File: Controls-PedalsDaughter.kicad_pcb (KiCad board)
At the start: 2 copper layers, 40 x 50 mm, 37 parts, among them J2 Accel Pos. Sensor, J3 PeripheralCANConnector, J4 Conn_01x02, J5 PeripheralCANConnector, U1 RI3-1205S, U2 PeripheralSOM, U3 TLV9301xDCK, U4 AMC1300BDWV, U5 TLV70130DBVR

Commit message: again
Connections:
- D1 pad 1: +3.3V -> +3V3
- D3 pad 1: +3.3V -> +3V3
- U2 pad 2: +3.3V -> +3V3
- U2 pad 9: +3.3V -> +3V3
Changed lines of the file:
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@@
 	(net 7 "+3V3PWR")
 	(net 8 "+3V3")
-	(net 9 "+3.3V")
-	(net 10 "Net-(D6-A)")
-	(net 11 "unconnected-(J2-Pin_2-Pad2)")
-	(net 12 "Net-(J2-Pin_5)")
-	(net 13 "/CAN_L")
-	(net 14 "/CAN_H")
-	(net 15 "/INP")
-	(net 16 "Net-(U3-+)")
-	(net 17 "unconnected-(U2-SPI1_NSS-Pad19)")
-	(net 18 "unconnected-(U2-I2C2_SCL-Pad8)")
-	(net 19 "unconnected-(U2-SPI1_MISO-Pad15)")
-	(net 20 "unconnected-(U2-VDDA(3.3V)-Pad10)")
-	(net 21 "unconnected-(U2-SPI2_NSS-Pad7)")
-	(net 22 "unconnected-(U2-GNDA-Pad12)")
-	(net 23 "unconnected-(U2-SPI1_SCK-Pad13)")
-	(net 24 "unconnected-(U2-SPI2_MOSI-Pad1)")
-	(net 25 "unconnected-(U2-SPI2_MISO-Pad3)")
-	(net 26 "unconnected-(U2-I2C1_SDA-Pad16)")
-	(net 27 "unconnected-(U2-I2C2_SDA-Pad6)")
-	(net 28 "unconnected-(U2-SPI2_SCK-Pad5)")
-	(net 29 "unconnected-(U2-SPI1_MOSI-Pad17)")
-	(net 30 "unconnected-(U2-I2C1_SCL-Pad14)")
-	(net 31 "unconnected-(U5-NC-Pad3)")
-	(net 32 "unconnected-(U5-NC-Pad2)")
+	(net 9 "Net-(D6-A)")
+	(net 10 "unconnected-(J2-Pin_2-Pad2)")
+	(net 11 "Net-(J2-Pin_5)")
+	(net 12 "/CAN_L")
+	(net 13 "/CAN_H")
+	(net 14 "/INP")
+	(net 15 "Net-(U3-+)")
+	(net 16 "unconnected-(U2-SPI1_NSS-Pad19)")
+	(net 17 "unconnected-(U2-I2C2_SCL-Pad8)")
+	(net 18 "unconnected-(U2-SPI1_MISO-Pad15)")
+	(net 19 "unconnected-(U2-VDDA(3.3V)-Pad10)")
+	(net 20 "unconnected-(U2-SPI2_NSS-Pad7)")
+	(net 21 "unconnected-(U2-GNDA-Pad12)")
+	(net 22 "unconnected-(U2-SPI1_SCK-Pad13)")
+	(net 23 "unconnected-(U2-SPI2_MOSI-Pad1)")
+	(net 24 "unconnected-(U2-SPI2_MISO-Pad3)")
+	(net 25 "unconnected-(U2-I2C1_SDA-Pad16)")
+	(net 26 "unconnected-(U2-I2C2_SDA-Pad6)")
+	(net 27 "unconnected-(U2-SPI2_SCK-Pad5)")
+	(net 28 "unconnected-(U2-SPI1_MOSI-Pad17)")
+	(net 29 "unconnected-(U2-I2C1_SCL-Pad14)")
+	(net 30 "unconnected-(U5-NC-Pad3)")
+	(net 31 "unconnected-(U5-NC-Pad2)")
 	(footprint "TestPoint:TestPoint_Pad_1.5x1.5mm"
 		(layer "F.Cu")
@@
 			(layers "*.Cu" "*.Mask")
 			(remove_unused_layers no)
-			(net 14 "/CAN_H")
+			(net 13 "/CAN_H")
 			(pinfunction "CAN_H")
 			(pintype "bidirectional")
@@
 			(layers "*.Cu" "*.Mask")
 			(remove_unused_layers no)
-			(net 13 "/CAN_L")
+			(net 12 "/CAN_L")
 			(pinfunction "CAN_L")
 			(pintype "bidirectional")
@@
 			(layers "F.Cu" "F.Paste" "F.Mask")
 			(roundrect_rratio 0.25)
-			(net 16 "Net-(U3-+)")
+			(net 15 "Net-(U3-+)")
 			(pinfunction "+")
 			(pintype "input")
@@
 			(layers "F.Cu" "F.Paste" "F.Mask")
 			(roundrect_rratio 0.25)
-			(net 32 "unconnected-(U5-NC-Pad2)")
+			(net 31 "unconnected-(U5-NC-Pad2)")
 			(pinfunction "NC")
 			(pintype "unspecified+no_connect")
@@
 			(layers "F.Cu" "F.Paste" "F.Mask")
 			(roundrect_rratio 0.25)
-			(net 31 "unconnected-(U5-NC-Pad3)")
+			(net 30 "unconnected-(U5-NC-Pad3)")
 			(pinfunction "NC")
 			(pintype "unspecified+no_connect")
@@
 			(layers "*.Cu" "*.Mask")
 			(remove_unused_layers no)
-			(net 11 "unconnected-(J2-Pin_2-Pad2)")
+			(net 10 "unconnected-(J2-Pin_2-Pad2)")
 			(pinfunction "Pin_2")
 			(pintype "passive+no_connect")
@@
 			(layers "*.Cu" "*.Mask")
 			(remove_unused_layers no)
-			(net 12 "Net-(J2-Pin_5)")
+			(net 11 "Net-(J2-Pin_5)")
 			(pinfunction "Pin_5")
 			(pintype "passive")
@@
 			(layers "*.Cu" "*.Mask")
 			(remove_unused_layers no)
-			(net 14 "/CAN_H")
+			(net 13 "/CAN_H")
 			(pinfunction "CAN_H")
 			(pintype "bidirectional")
@@
 			(layers "*.Cu" "*.Mask")
 			(remove_unused_layers no)
-			(net 13 "/CAN_L")
+			(net 12 "/CAN_L")
 			(pinfunction "CAN_L")
 			(pintype "bidirectional")
@@
 			(layers "F.Cu" "F.Paste" "F.Mask")
 			(roundrect_rratio 0.25)
-			(net 15 "/INP")
+			(net 14 "/INP")
 			(pinfunction "+")
 			(pintype "input")
@@
 			(layers "F.Cu" "F.Paste" "F.Mask")
 			(roundrect_rratio 0.25)
-			(net 10 "Net-(D6-A)")
+			(net 9 "Net-(D6-A)")
 			(pinfunction "A")
 			(pintype "passive")
@@
 			(layers "*.Cu" "*.Mask")
 			(remove_unused_layers no)
-			(net 15 "/INP")
+			(net 14 "/INP")
 			(pinfunction "Pin_2")
 			(pintype "passive")
@@
 			(layers "B.Cu" "B.Paste" "B.Mask")
 			(roundrect_rratio 0.25)
-			(net 9 "+3.3V")
+			(net 8 "+3V3")
 			(pinfunction "K")
 			(pintype "passive")
@@
 			(layers "B.Cu" "B.Paste" "B.Mask")
 			(roundrect_rratio 0.243902)
-			(net 16 "Net-(U3-+)")
+			(net 15 "Net-(U3-+)")
 			(pintype "passive")
 		)
@@
 			(layers "B.Cu" "B.Paste" "B.Mask")
 			(roundrect_rratio 0.243902)
-			(net 12 "Net-(J2-Pin_5)")
+			(net 11 "Net-(J2-Pin_5)")
 			(pintype "passive")
 		)
@@
 			(layers "B.Cu" "B.Paste" "B.Mask")
 			(roundrect_rratio 0.243902)
-			(net 16 "Net-(U3-+)")
+			(net 15 "Net-(U3-+)")
 			(pintype "passive")
 		)
@@
 			(layers "B.Cu" "B.Paste" "B.Mask")
 			(roundrect_rratio 0.243902)
-			(net 10 "Net-(D6-A)")
+			(net 9 "Net-(D6-A)")
 			(pintype "passive")
 		)
@@
 			(layers "B.Cu" "B.Paste" "B.Mask")
 			(roundrect_rratio 0.243902)
-			(net 15 "/INP")
+			(net 14 "/INP")
 			(pintype "passive")
 		)
@@
 		(fp_arc
 			(start 21.237742 18.612258)
-			(mid 20.300482 20.874999)
+			(mid 20.300481 20.874995)
 			(end 18.037742 21.812258)
 			(stroke
@@
 			(size 0.55 1.8)
 			(layers "B.Cu" "B.Paste" "B.Mask")
-			(net 24 "unconnected-(U2-SPI2_MOSI-Pad1)")
+			(net 23 "unconnected-(U2-SPI2_MOSI-Pad1)")
 			(pinfunction "SPI2_MOSI")
 			(pintype "passive+no_connect")
 		)
 		(pad "2" smd rect
-			(at 20.475 1.175 90)
+			(at 20.475 1.175 270)
 			(size 0.55 1.8)
 			(layers "B.Cu" "B.Paste" "B.Mask")
-			(net 9 "+3.3V")
+			(net 8 "+3V3")
 			(pinfunction "+3.3V")
 			(pintype "passive")
@@
 			(size 0.55 1.8)
 			(layers "B.Cu" "B.Paste" "B.Mask")
-			(net 25 "unconnected-(U2-SPI2_MISO-Pad3)")
+			(net 24 "unconnected-(U2-SPI2_MISO-Pad3)")
 			(pinfunction "SPI2_MISO")
 			(pintype "passive+no_connect")
@@
 			(size 0.55 1.8)
 			(layers "B.Cu" "B.Paste" "B.Mask")
-			(net 28 "unconnected-(U2-SPI2_SCK-Pad5)")
+			(net 27 "unconnected-(U2-SPI2_SCK-Pad5)")
 			(pinfunction "SPI2_SCK")
 			(pintype "passive+no_connect")
@@
 			(size 0.55 1.8)
 			(layers "B.Cu" "B.Paste" "B.Mask")
-			(net 27 "unconnected-(U2-I2C2_SDA-Pad6)")
+			(net 26 "unconnected-(U2-I2C2_SDA-Pad6)")
 			(pinfunction "I2C2_SDA")
 			(pintype "passive+no_connect")
@@
 			(size 0.55 1.8)
 			(layers "B.Cu" "B.Paste" "B.Mask")
-			(net 21 "unconnected-(U2-SPI2_NSS-Pad7)")
+			(net 20 "unconnected-(U2-SPI2_NSS-Pad7)")
 			(pinfunction "SPI2_NSS")
 			(pintype "passive+no_connect")
@@
 			(size 0.55 1.8)
 			(layers "B.Cu" "B.Paste" "B.Mask")
-			(net 18 "unconnected-(U2-I2C2_SCL-Pad8)")
+			(net 17 "unconnected-(U2-I2C2_SCL-Pad8)")
 			(pinfunction "I2C2_SCL")
 			(pintype "passive+no_connect")
 		)
 		(pad "9" smd rect
-			(at 16.175 -2.025 90)
+			(at 16.175 -2.025 270)
 			(size 0.55 1.8)
 			(layers "B.Cu" "B.Paste" "B.Mask")
-			(net 9 "+3.3V")
+			(net 8 "+3V3")
 			(pinfunction "+3.3V")
 			(pintype "output")
@@
 			(size 0.55 1.8)
 			(layers "B.Cu" "B.Paste" "B.Mask")
-			(net 20 "unconnected-(U2-VDDA(3.3V)-Pad10)")
+			(net 19 "unconnected-(U2-VDDA(3.3V)-Pad10)")
 			(pinfunction "VDDA(3.3V)")
 			(pintype "passive+no_connect")
@@
 			(size 0.55 1.8)
 			(layers "B.Cu" "B.Paste" "B.Mask")
-			(net 22 "unconnected-(U2-GNDA-Pad12)")
+			(net 21 "unconnected-(U2-GNDA-Pad12)")
 			(pinfunction "GNDA")
 			(pintype "output+no_connect")
@@
 			(size 0.55 1.8)
 			(layers "B.Cu" "B.Paste" "B.Mask")
-			(net 23 "unconnected-(U2-SPI1_SCK-Pad13)")
+			(net 22 "unconnected-(U2-SPI1_SCK-Pad13)")
 			(pinfunction "SPI1_SCK")
 			(pintype "passive+no_connect")
@@
 			(size 0.55 1.8)
 			(layers "B.Cu" "B.Paste" "B.Mask")
-			(net 30 "unconnected-(U2-I2C1_SCL-Pad14)")
+			(net 29 "unconnected-(U2-I2C1_SCL-Pad14)")
 			(pinfunction "I2C1_SCL")
 			(pintype "passive+no_connect")
@@
 			(size 0.55 1.8)
 			(layers "B.Cu" "B.Paste" "B.Mask")
-			(net 19 "unconnected-(U2-SPI1_MISO-Pad15)")
+			(net 18 "unconnected-(U2-SPI1_MISO-Pad15)")
 			(pinfunction "SPI1_MISO")
 			(pintype "passive+no_connect")
@@
 			(size 0.55 1.8)
 			(layers "B.Cu" "B.Paste" "B.Mask")
-			(net 26 "unconnected-(U2-I2C1_SDA-Pad16)")
+			(net 25 "unconnected-(U2-I2C1_SDA-Pad16)")
 			(pinfunction "I2C1_SDA")
 			(pintype "passive+no_connect")
@@
 			(size 0.55 1.8)
 			(layers "B.Cu" "B.Paste" "B.Mask")
-			(net 29 "unconnected-(U2-SPI1_MOSI-Pad17)")
+			(net 28 "unconnected-(U2-SPI1_MOSI-Pad17)")
 			(pinfunction "SPI1_MOSI")
 			(pintype "passive+no_connect")
@@
 			(size 0.55 1.8)
 			(layers "B.Cu" "B.Paste" "B.Mask")
-			(net 17 "unconnected-(U2-SPI1_NSS-Pad19)")
+			(net 16 "unconnected-(U2-SPI1_NSS-Pad19)")
 			(pinfunction "SPI1_NSS")
 			(pintype "passive+no_connect")
@@
 			(size 0.55 1.8)
 			(layers "B.Cu" "B.Paste" "B.Mask")
-			(net 13 "/CAN_L")
+			(net 12 "/CAN_L")
 			(pinfunction "CAN_L")
 			(pintype "passive")
@@
 			(size 0.55 1.8)
 			(layers "B.Cu" "B.Paste" "B.Mask")
-			(net 14 "/CAN_H")
+			(net 13 "/CAN_H")
 			(pinfunction "CAN_H")
 			(pintype "passive")
@@
 			(layers "B.Cu" "B.Paste" "B.Mask")
 			(roundrect_rratio 0.25)
-			(net 9 "+3.3V")
+			(net 8 "+3V3")
 			(pinfunction "K")
 			(pintype "passive")

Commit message: Yuh
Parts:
- added Accel_Raw1: Accel_Raw_TP, TestPoint:TestPoint_THTPad_1.5x1.5mm_Drill0.7mm, F.Cu at (101.8, 76.5)
- added Accel_TP1: Accel, TestPoint:TestPoint_THTPad_1.5x1.5mm_Drill0.7mm, F.Cu at (106.6, 67.5)
- added Brake_Fl_Sn1: Brake_Fl_Sn_TP, TestPoint:TestPoint_THTPad_1.5x1.5mm_Drill0.7mm, F.Cu at (123.0, 66.8)
- added Brake_Fl_Sn_Raw1: Brake_Fl_Sn_Raw_TP, TestPoint:TestPoint_THTPad_1.5x1.5mm_Drill0.7mm, F.Cu at (124.2, 47.0)
- added Brake_Raw1: Brake_Raw_TP, TestPoint:TestPoint_THTPad_1.5x1.5mm_Drill0.7mm, F.Cu at (101.8, 50.2)
- added Brake_TP1: Brake, TestPoint:TestPoint_THTPad_1.5x1.5mm_Drill0.7mm, F.Cu at (106.5, 59.0)
- added C13: 0.1uf, Capacitor_SMD:C_0805_2012Metric, F.Cu at (109.1, 53.7)
- added C14: 1nf, Capacitor_SMD:C_0805_2012Metric, F.Cu at (104.1, 53.7)
- added D5: MBR, Diode_SMD:D_0805_2012Metric, F.Cu at (104.8, 56.5)
- added D8: MBR, Diode_SMD:D_0805_2012Metric, F.Cu at (108.4, 56.5)
- added J1: Brake Pos. Sensor, Connector_Molex:Molex_Micro-Fit_3.0_43045-0612_2x03_P3.00mm_Vertical, F.Cu at (104.6, 41.5)
- added R5: 8.2k, Resistor_SMD:R_0805_2012Metric, F.Cu at (107.5, 50.2)
- added R6: 22k, Resistor_SMD:R_0805_2012Metric, F.Cu at (105.5, 50.2)
- added U6: TLV9301xDCK, Package_TO_SOT_SMD:SOT-353_SC-70-5, F.Cu at (106.6, 53.7)
- C1: value 1nF -> 100nF; moved to F.Cu
- C10: value 1nF -> 1uF; moved to F.Cu
- C11: value 100nF -> 100uF; moved to F.Cu
- C12: value 0.1uf -> 1nf; moved to F.Cu
- C2, C4, C5, C6, C7, D1, D2, D3, D4, R1, R2, R3, R4: moved to F.Cu
- C3: value 1nf -> 0.1uf; moved to F.Cu
- C8: value 1uF -> 1nF; moved to F.Cu
- C9: value 100uF -> 1nF; moved to F.Cu
- D6: value SMD_0805 -> PESD15VL1BA; footprint Diode_SMD:D_0805_2012Metric -> Diode_SMD:D_SOD-323
- D7: value PESD15VL1BA -> SMD_0805; footprint Diode_SMD:D_SOD-323 -> Diode_SMD:D_0805_2012Metric; moved to F.Cu
- U4: value AMC1300BDWV -> TLV70130DBVR; footprint Package_SO:SOIC-8_7.5x5.85mm_P1.27mm -> Package_TO_SOT_SMD:SOT-353_SC-70-5
- U5: value TLV70130DBVR -> AMC1300BDWV; footprint Package_TO_SOT_SMD:SOT-353_SC-70-5 -> Package_SO:SOIC-8_7.5x5.85mm_P1.27mm
- moved J2 41.2 mm to (110.5, 85.0), turned to 180 degrees
- moved D6 40.7 mm to (122.8, 78.8), turned to 180 degrees
- moved J4 34.5 mm to (119.5, 41.5), turned to 0 degrees
- moved R3 34.0 mm to (117.6, 74.2), turned to 0 degrees
- moved GND1 33.9 mm to (119.7, 78.5), turned to 90 degrees
- moved R4 32.7 mm to (105.6, 76.2), turned to -90 degrees
- moved +12V1 30.5 mm to (126.8, 67.8), turned to 0 degrees
- moved C3 29.9 mm to (104.1, 72.8), turned to 90 degrees
- moved R2 29.8 mm to (107.6, 76.2), turned to -90 degrees
- moved R1 29.4 mm to (120.5, 47.2), turned to 180 degrees
- moved U1 26.5 mm to (120.7, 81.5), turned to 180 degrees
- moved D2 25.9 mm to (104.8, 70.0), turned to 180 degrees
- moved C7 25.9 mm to (124.5, 49.6)
- moved U3 25.2 mm to (106.6, 72.8), turned to 90 degrees
- moved +5V1 24.4 mm to (114.5, 74.0), turned to 90 degrees
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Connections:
- C1 pad 1: /Brake -> +12V
- C1 pad 2: GND -> GNDPWR
- C10 pad 1: +3V3PWR -> +3V3
- C10 pad 2: GNDPWR -> GND
- C11 pad 1: +12V -> +3V3
- C11 pad 2: GNDPWR -> GND
- C12 pad 2: +5V -> /Accel
- C3 pad 2: /Accel -> +5V
- C8 pad 1: +3V3 -> +3V3PWR
- C8 pad 2: GND -> GNDPWR
- C9 pad 1: +3V3 -> /Brake_Fl
- D3 pad 2: /Brake -> /Brake_Fl
- D4 pad 1: /Brake -> /Brake_Fl
- D6 pad 1: GND -> GNDPWR
- D6 pad 2: Net-(D6-A) -> +12V
- D7 pad 1: GNDPWR -> GND
- D7 pad 2: +12V -> Net-(D7-A)
- J4 pad 2: /INP -> /Brake Fluid Sensor/INP
- R1 pad 1: /INP -> /Brake Fluid Sensor/INP
- R3 pad 2: Net-(D6-A) -> Net-(D7-A)
- U2 pad 19: unconnected-(U2-SPI1_NSS-Pad19) -> /Brake_Fl
- U2 pad 20: /Brake -> /Brake_Pot
- U4 pad 1: +3V3PWR -> +12V
- U4 pad 2: /INP -> unconnected-(U4-NC-Pad2)
- U4 pad 3: GNDPWR -> unconnected-(U4-NC-Pad3)
- U4 pad 5: GND -> +3V3PWR
- U5 pad 1: +12V -> +3V3PWR
- U5 pad 2: unconnected-(U5-NC-Pad2) -> /Brake Fluid Sensor/INP
- U5 pad 3: unconnected-(U5-NC-Pad3) -> GNDPWR
- U5 pad 5: +3V3PWR -> GND

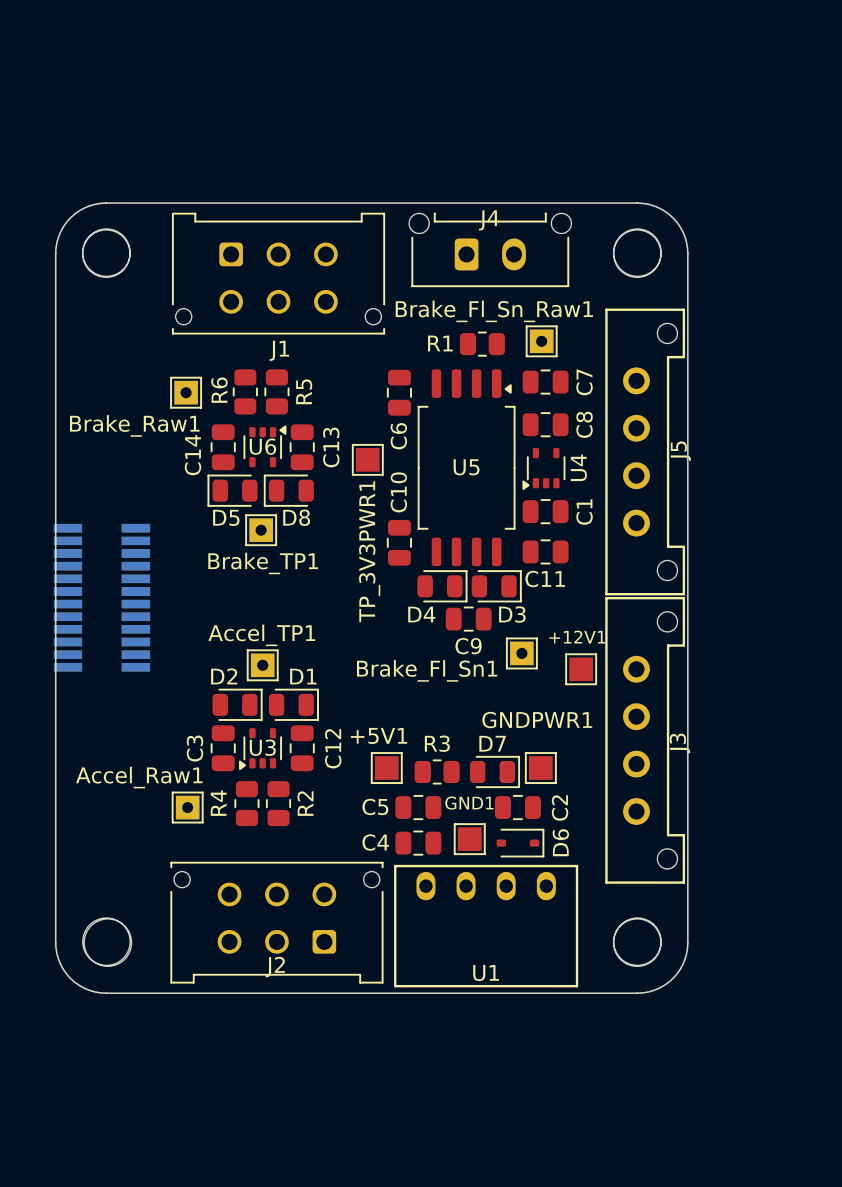
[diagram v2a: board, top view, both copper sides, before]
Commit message: expanded board, and made all things go one way
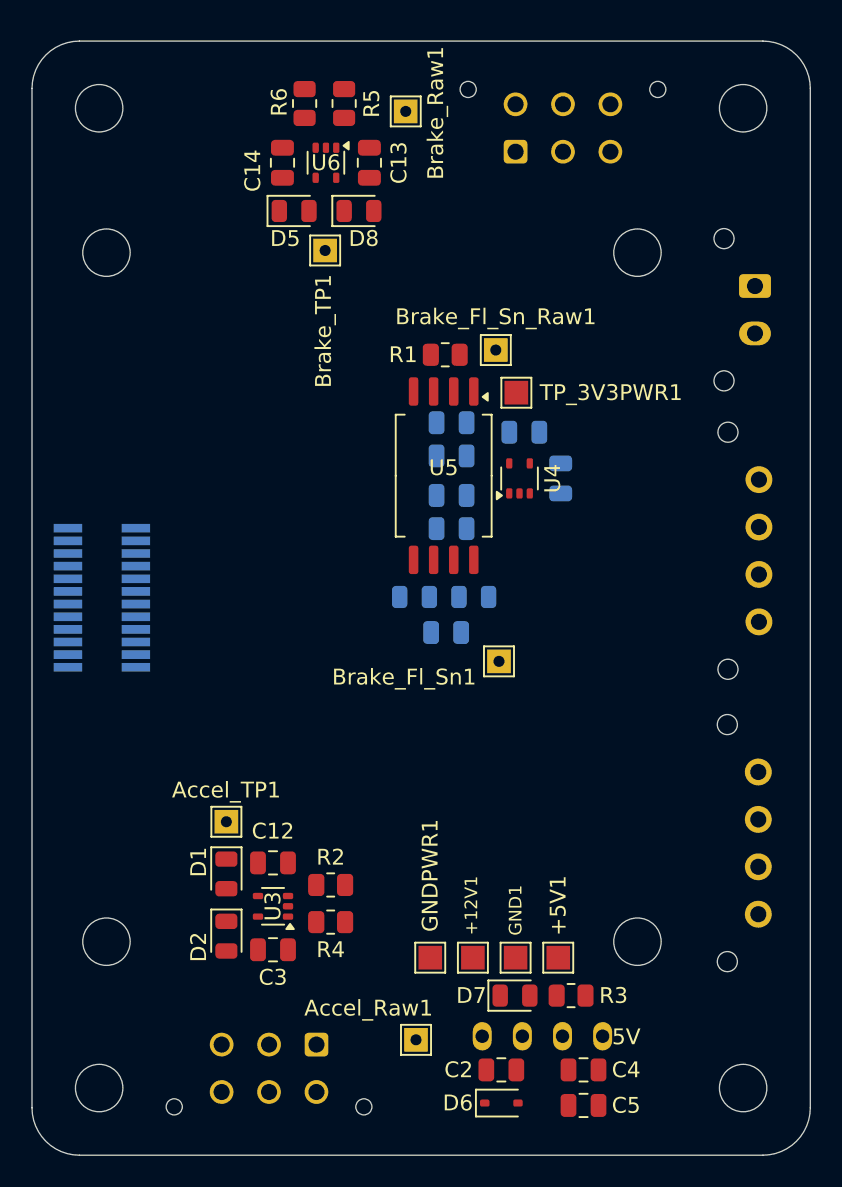
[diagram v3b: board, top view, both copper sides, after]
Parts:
- removed the ? at (113.5, 38.2)
- added ?: , clipboard:1102f6bf-9d39-4637-903a-16b78c874ac5, F.Cu at (99.5, 32.2)
- added ?: , clipboard:1102f6bf-9d39-4637-903a-16b78c874ac5, F.Cu at (140.2, 32.2)
- added ?: , clipboard:1102f6bf-9d39-4637-903a-16b78c874ac5, F.Cu at (99.5, 94.2)
- added ?: , clipboard:1102f6bf-9d39-4637-903a-16b78c874ac5, F.Cu at (140.2, 94.2)
- C1, C10, C11, C6, C7, C8, C9, D3, D4, J1, J2, J3, J4, J5, U1: moved to B.Cu
- moved Brake_Raw1 22.6 mm to (115.7, 32.5)
- moved C5 21.6 mm to (126.9, 95.3), turned to 180 degrees
- moved Accel_Raw1 20.6 mm to (116.3, 91.2)
- moved +12V1 19.5 mm to (119.9, 86.0)
- moved J1 19.1 mm to (122.6, 35.0)
- moved R5 18.7 mm to (111.8, 31.9)
- moved R6 18.6 mm to (109.2, 31.9)
- moved C13 18.5 mm to (113.3, 35.7)
- moved U6 18.4 mm to (110.6, 35.7)
- moved C14 18.4 mm to (107.8, 35.7)
- moved J4 18.4 mm to (137.8, 43.5), turned to -90 degrees
- moved D8 18.2 mm to (112.7, 38.8)
- moved Brake_TP1 18.2 mm to (110.5, 41.2)
- moved D5 18.1 mm to (108.6, 38.8)
- moved C4 17.8 mm to (126.9, 93.1), turned to 180 degrees
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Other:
- board size 40 x 50 mm -> 49.2 x 70.5 mm
- board text added: "5V"

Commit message: errrrrrrkereoem
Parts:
- Accel_Raw1, Accel_TP1, Brake_Fl_Sn1, Brake_Fl_Sn_Raw1, Brake_Raw1, Brake_TP1, C12, C13, C14, C3, D1, D2, D5, D7, D8, R1, R2, R3, R4, R5, R6, U3, U4, U5, U6: moved to B.Cu
- C10, C11, C6, C7: moved to F.Cu
- moved Brake_Fl_Sn1 31.4 mm to (134.2, 38.5)
- moved Brake_Fl_Sn_Raw1 20.4 mm to (139.5, 38.2), turned to -90 degrees
- moved R6 15.9 mm to (119.5, 44.1), turned to 0 degrees
- moved TP_3V3PWR1 15.2 mm to (130.5, 63.2), turned to 90 degrees
- moved Accel_TP1 13.6 mm to (98.5, 89.8)
- moved C14 12.6 mm to (115.8, 45.5), turned to 0 degrees
- moved R5 12.4 mm to (119.5, 41.6), turned to 0 degrees
- moved C8 11.2 mm to (131.4, 60.3)
- moved Brake_TP1 9.96 mm to (113.0, 31.6), turned to 90 degrees
- moved U4 8.95 mm to (131.7, 57.3), turned to -90 degrees
- moved U6 8.73 mm to (115.8, 42.8), turned to 180 degrees
- moved D5 7.28 mm to (112.7, 44.8), turned to 90 degrees
- moved D2 7.01 mm to (109.1, 79.6), turned to 0 degrees
- moved R2 6.91 mm to (105.9, 86.2), turned to -90 degrees
- moved C1 6.10 mm to (131.4, 54.3), turned to 0 degrees
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
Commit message: thanks ravi <3
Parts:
- +12V1, +5V1, GND1, GNDPWR1, TP_3V3PWR1: moved to B.Cu
- moved GND1 60.1 mm to (162.3, 131.1), turned to 0 degrees
- moved +5V1 56.4 mm to (162.3, 128.5)
- moved J3 55.0 mm to (168.5, 120.0), turned to 90 degrees
- moved J5 54.8 mm to (168.5, 101.3), turned to 90 degrees
- moved GNDPWR1 54.3 mm to (147.4, 131.1), turned to 0 degrees
- moved C1 52.5 mm to (161.7, 97.2), turned to 180 degrees
- moved +12V1 50.6 mm to (147.4, 128.5), turned to 180 degrees
- moved J4 50.6 mm to (168.6, 83.6), turned to 90 degrees
- moved D6 50.4 mm to (152.2, 133.2)
- moved C10 49.3 mm to (153.5, 95.8)
- moved R4 48.7 mm to (140.2, 122.9)
- moved C4 48.7 mm to (157.4, 131.1)
- moved C5 48.6 mm to (157.4, 133.2)
- moved U1 48.6 mm to (154.8, 128.8)
- moved J1 48.6 mm to (158.9, 67.3), turned to 180 degrees
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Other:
- board size 49.2 x 70.5 mm -> 49.2 x 71.5 mm
